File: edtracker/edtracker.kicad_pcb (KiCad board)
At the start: 2 copper layers, 36.8 x 36.8 mm, 3 parts, among them SW1 SW_Push_Dual

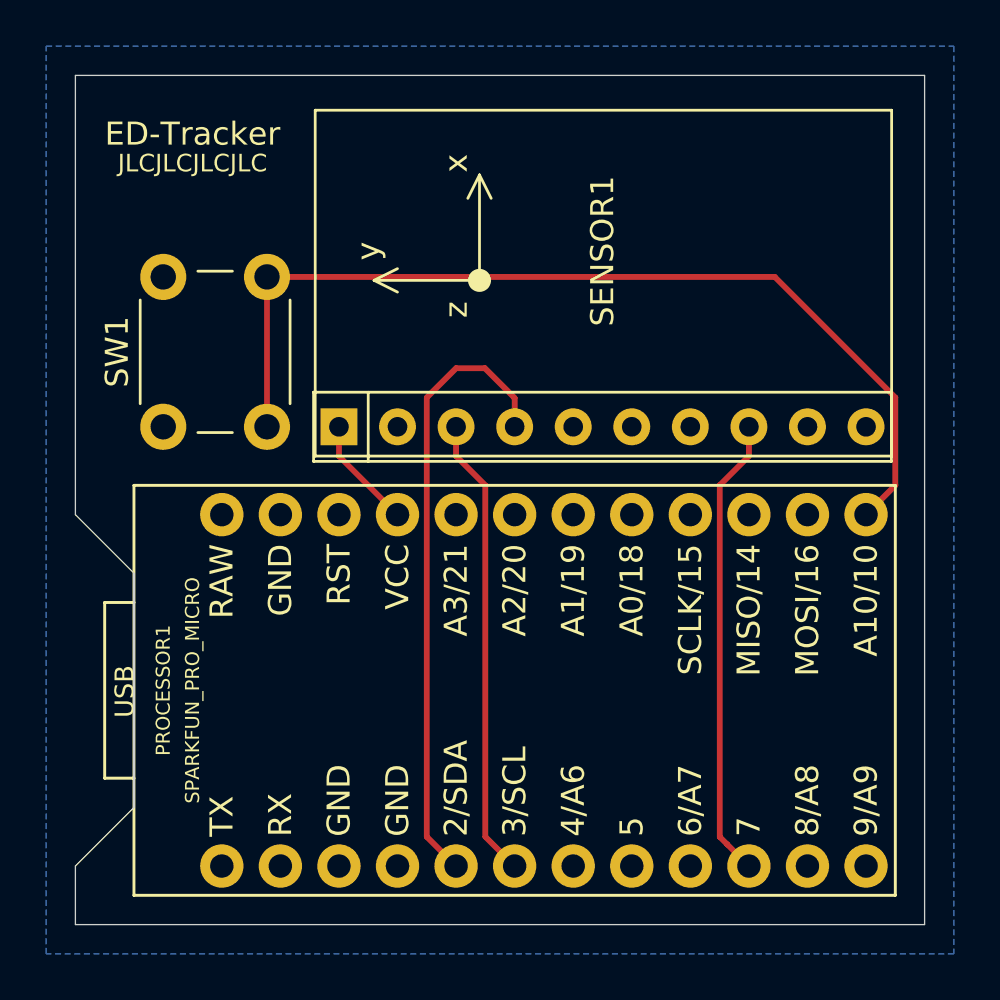
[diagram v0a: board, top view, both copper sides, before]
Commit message: changed processor -> microprocessor updated silkscreen
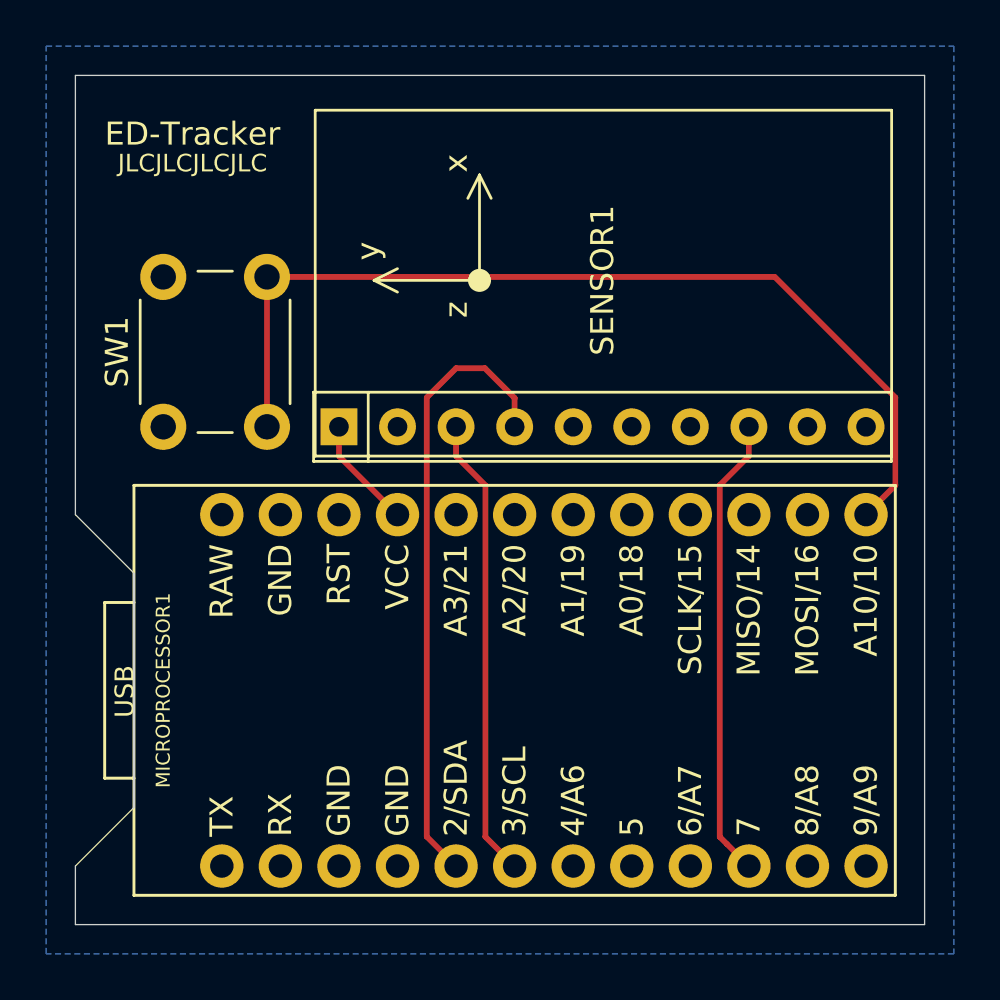
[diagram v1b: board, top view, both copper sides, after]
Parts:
- removed PROCESSOR1: SPARKFUN_PRO_MICRO, SparkFun_Boards:SPARKFUN_PRO_MICRO
- added MICROPROCESSOR1: SPARKFUN_PRO_MICRO, SparkFun_Boards:SPARKFUN_PRO_MICRO, F.Cu at (160.0, 127.0)

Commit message: Added open hardware logo and link to repo
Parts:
- added ?: , SparkFun_Aesthetics:OSHW-LOGO-MINI, F.Cu at (146.1, 105.4)
- added REF**: OSHW-Logo_7.5x8mm_SilkScreen, Symbol:OSHW-Logo_7.5x8mm_SilkScreen, B.Cu at (162.6, 105.4)
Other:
- board text added: "JLCJLCJLC"
- board text added: "https://github.com/FalcoGer/EdTracker_KiCad"
- board text removed: "JLCJLCJLCJLC"

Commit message: connected fsync to ground according to mpu spec
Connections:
- net Net-(MICROPROCESSOR1-Pad21) renamed +5V
- SENSOR1 pad 10: Net-(SENSOR1-Pad10) -> GND
